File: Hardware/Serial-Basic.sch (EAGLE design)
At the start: 24 parts, among them J1 microB, U1 AP2112-3.3V, U2 CH340G, Y2 12MHz

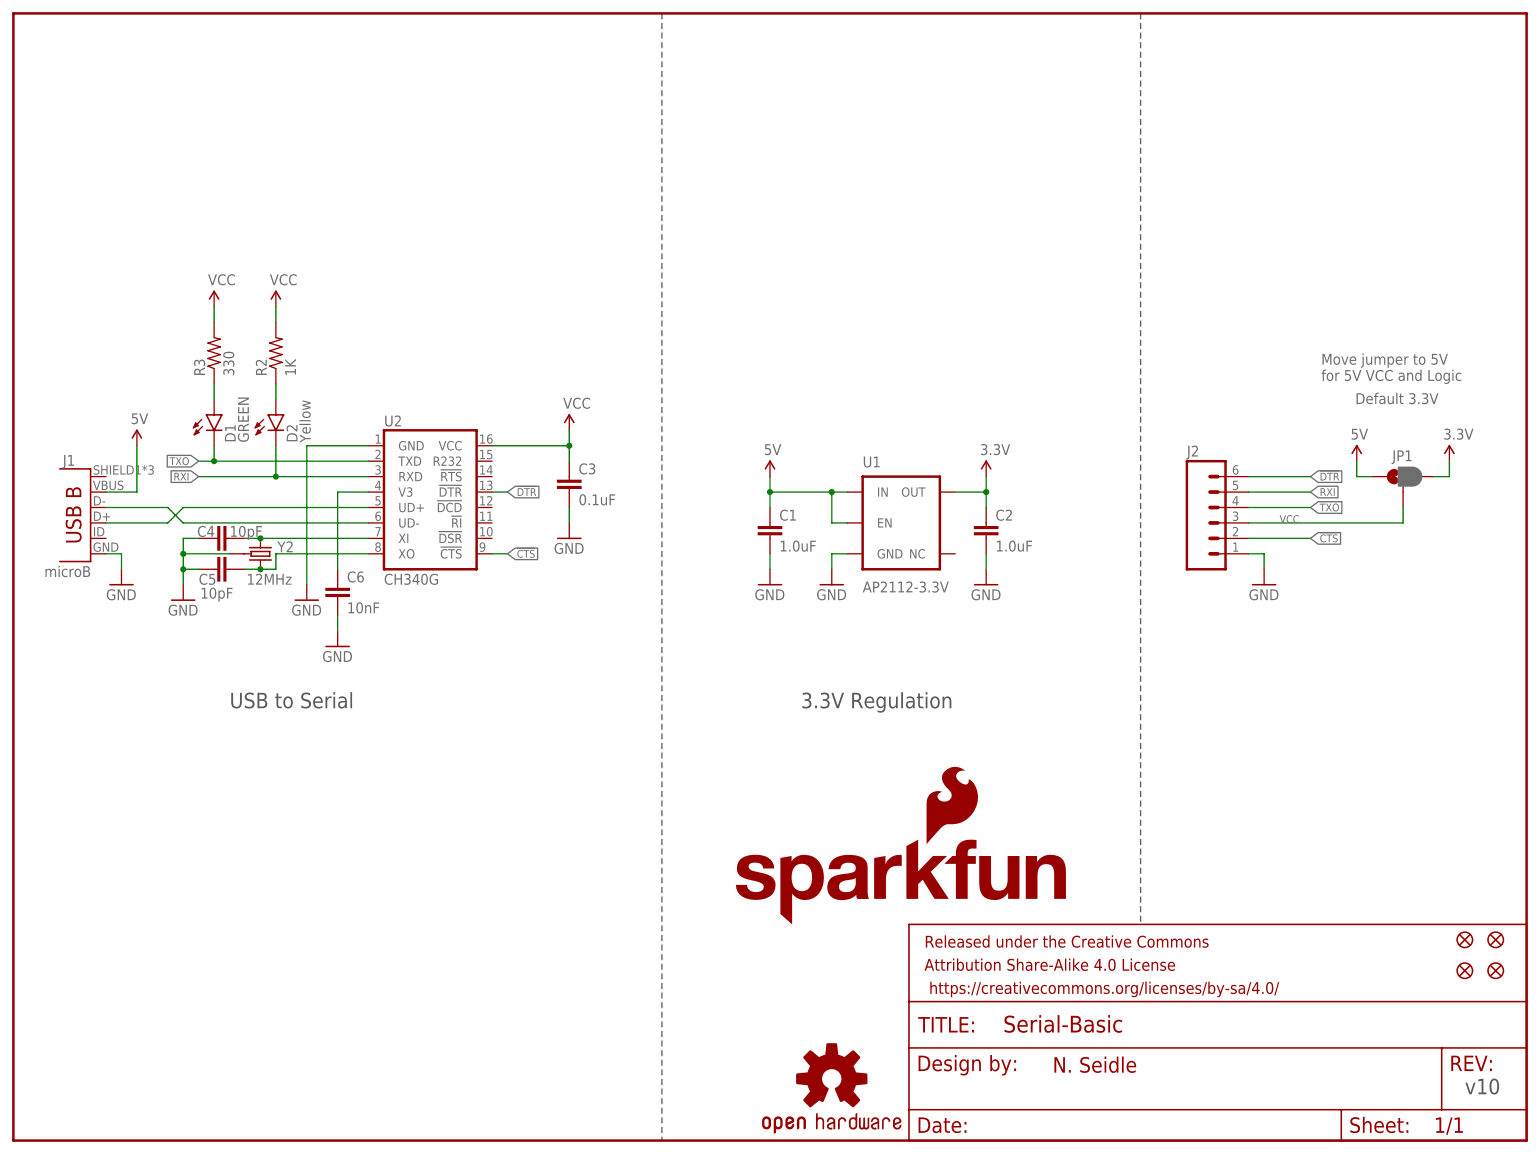
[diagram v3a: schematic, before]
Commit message: Adding buffer to RX line.
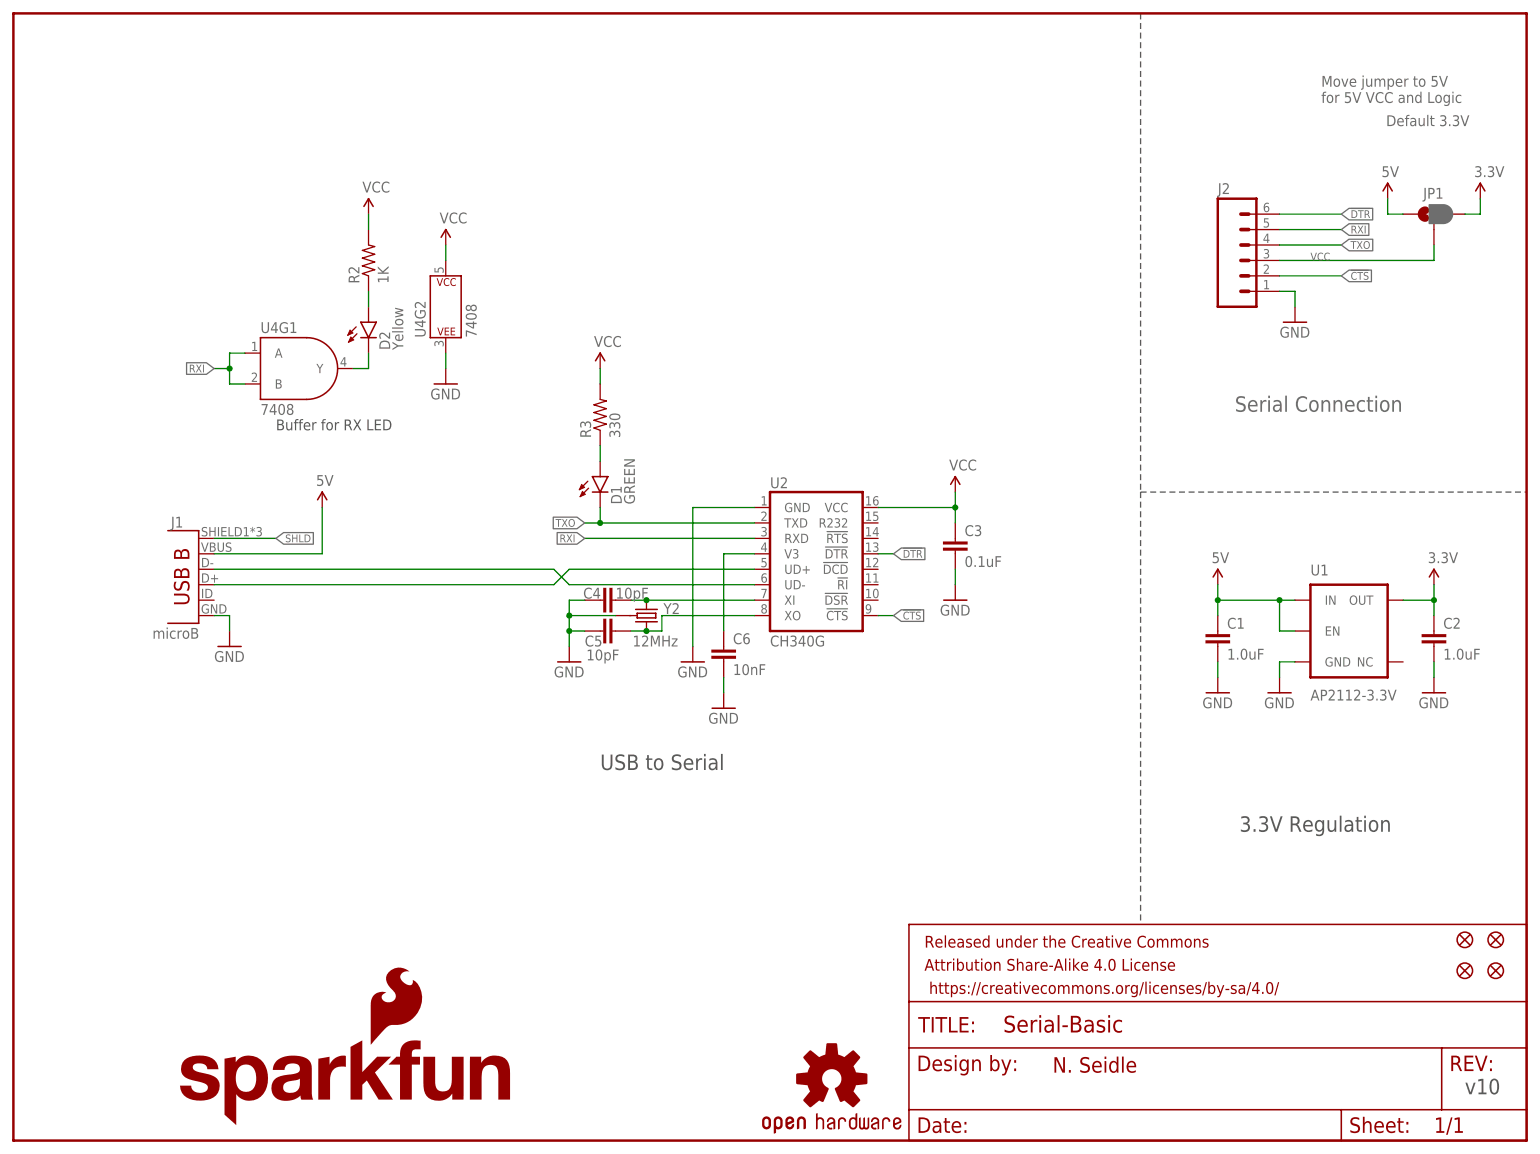
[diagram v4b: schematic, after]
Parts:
- added U4: 7408, Serial-Basic:7408
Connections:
- new net N$5: D2.C, U4G1.Y
- new net SHLD: J1.SHIELD
- net GND: now also U4G2.P$V-
- net RXI: now also U4G1.A, U4G1.B; no longer D2.C
- net VCC: now also U4G2.P$V+
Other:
- note added: "Buffer for RX LED"
- note added: "Serial Connection"
- moved on the sheet: C1, C2, C3, C4, C5, C6, D1, D2, J1, J2, JP1, R2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

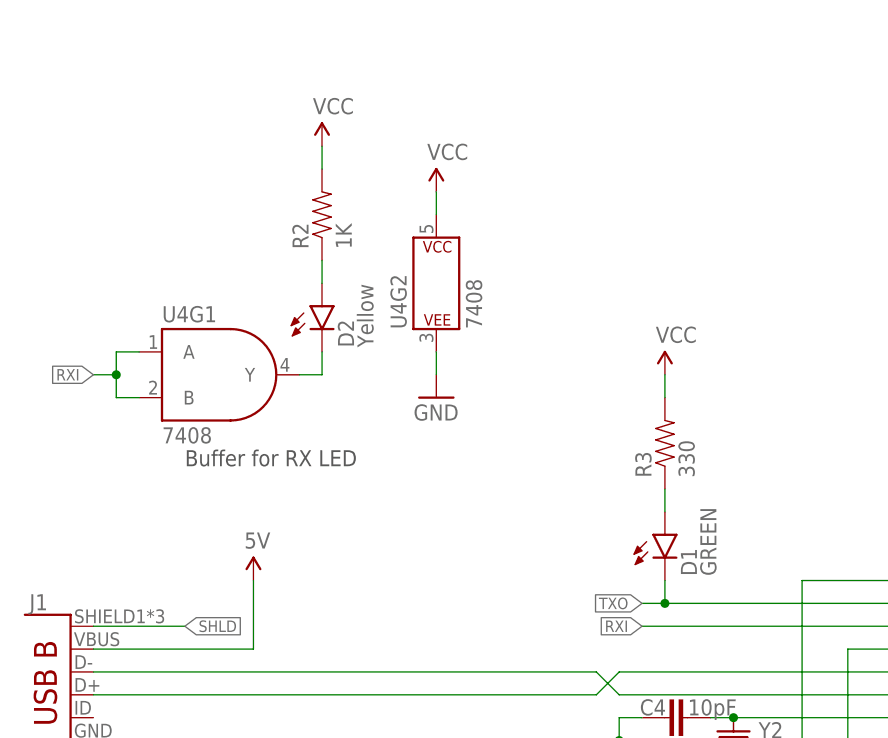
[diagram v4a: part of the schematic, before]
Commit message: Adding PROD_ID to AND gate
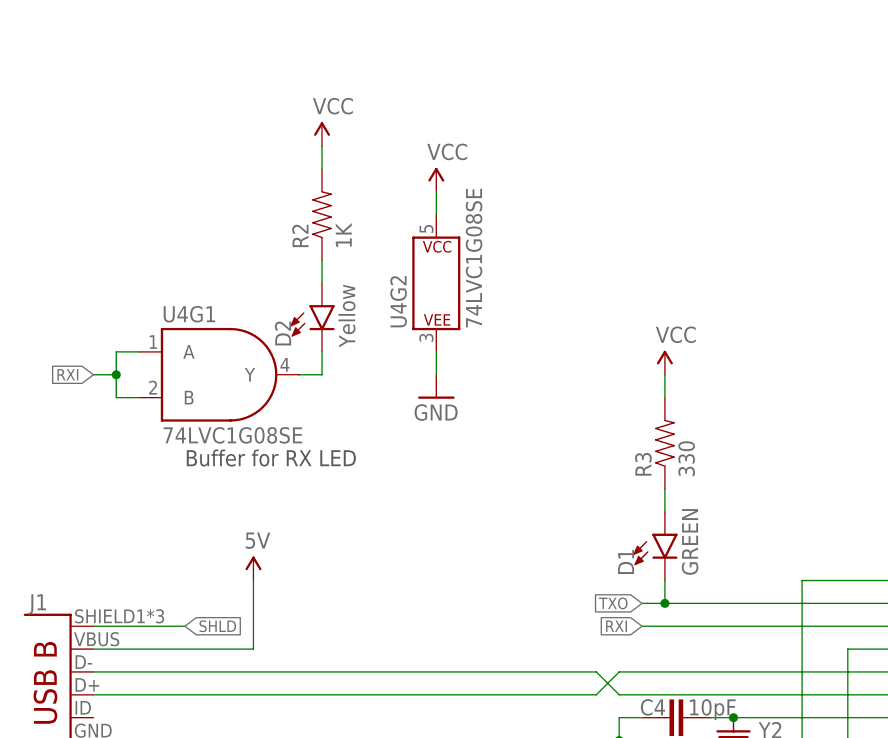
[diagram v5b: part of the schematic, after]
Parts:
- U4: value 7408 -> 74LVC1G08SE
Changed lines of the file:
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@@
 <?xml version="1.0" encoding="utf-8"?>
 <!DOCTYPE eagle SYSTEM "eagle.dtd">
-<eagle version="7.6.0">
+<eagle version="7.2.0">
 <drawing>
 <settings>
@@
 <part name="SUPPLY6" library="SparkFun-Aesthetics" deviceset="VCC" device=""/>
 <part name="GND10" library="SparkFun-Aesthetics" deviceset="GND" device=""/>
-<part name="U4" library="Serial-Basic" deviceset="74*08" device=""/>
+<part name="U4" library="Serial-Basic" deviceset="74*08" device="" value="74LVC1G08SE"/>
 </parts>
 <sheets>

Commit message: Add arrow to VCC net
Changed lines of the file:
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@@
 <?xml version="1.0" encoding="utf-8"?>
 <!DOCTYPE eagle SYSTEM "eagle.dtd">
-<eagle version="7.2.0">
+<eagle version="7.6.0">
 <drawing>
 <settings>
@@
 <part name="GND10" library="SparkFun-Aesthetics" deviceset="GND" device=""/>
 <part name="U4" library="Serial-Basic" deviceset="74*08" device="" value="74LVC1G08SE"/>
+<part name="SUPPLY7" library="SparkFun-Aesthetics" deviceset="VCC" device=""/>
 </parts>
 <sheets>
@@
 <instance part="U4" gate="G1" x="48.26" y="127"/>
 <instance part="U4" gate="G2" x="71.12" y="137.16"/>
+<instance part="SUPPLY7" gate="G$1" x="210.82" y="154.94"/>
 </instances>
 <busses>
@@
 <net name="VCC" class="0">
 <segment>
-<label x="213.36" y="144.78" size="1.27" layer="95"/>
 <pinref part="J2" gate="G$1" pin="3"/>
-<wire x1="208.28" y1="144.78" x2="233.68" y2="144.78" width="0.1524" layer="91"/>
+<wire x1="208.28" y1="144.78" x2="210.82" y2="144.78" width="0.1524" layer="91"/>
+<wire x1="210.82" y1="144.78" x2="233.68" y2="144.78" width="0.1524" layer="91"/>
 <wire x1="233.68" y1="144.78" x2="233.68" y2="147.32" width="0.1524" layer="91"/>
 <pinref part="JP1" gate="G$1" pin="2"/>
-</segment>
-<segment>
+<pinref part="SUPPLY7" gate="G$1" pin="VCC"/>
+<wire x1="210.82" y1="154.94" x2="210.82" y2="144.78" width="0.1524" layer="91"/>
+<junction x="210.82" y="144.78"/>
+</segment>
+<segment>
